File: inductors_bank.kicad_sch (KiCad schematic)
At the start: 38 parts, among them K301 HF3F-L-12-1ZL2T, K302 HF3F-L-12-1ZL2T, K303 HF3F-L-12-1ZL2T, K304 HF3F-L-12-1ZL2T, K305 HF3F-L-12-1ZL2T, K306 HF3F-L-12-1ZL2T, K307 HF3F-L-12-1ZL2T, Q301 PMOS, Q302 PMOS, Q303 NMOS, Q304 NMOS

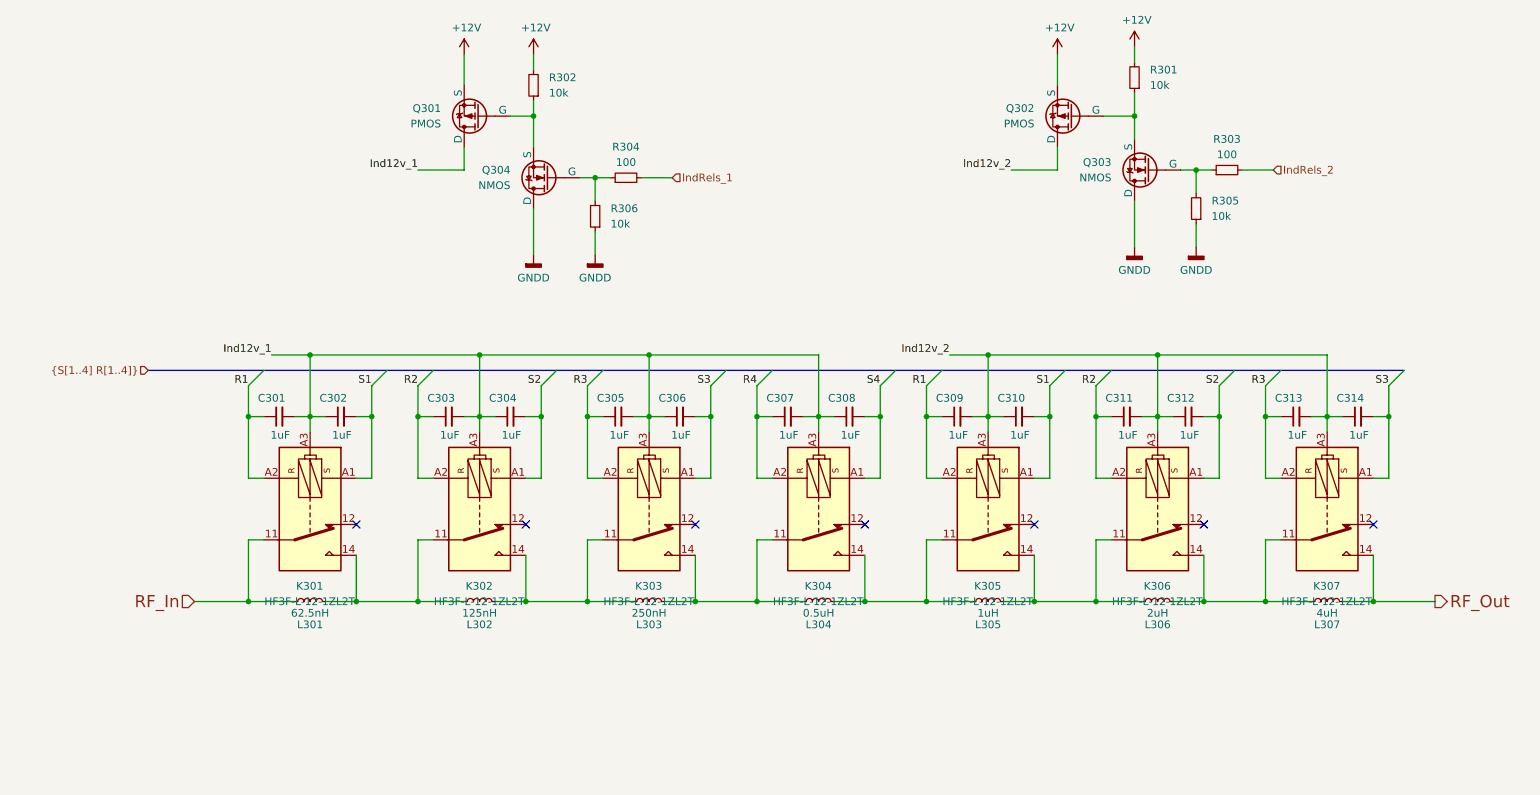
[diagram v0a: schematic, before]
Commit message: Added comments for inductors structure
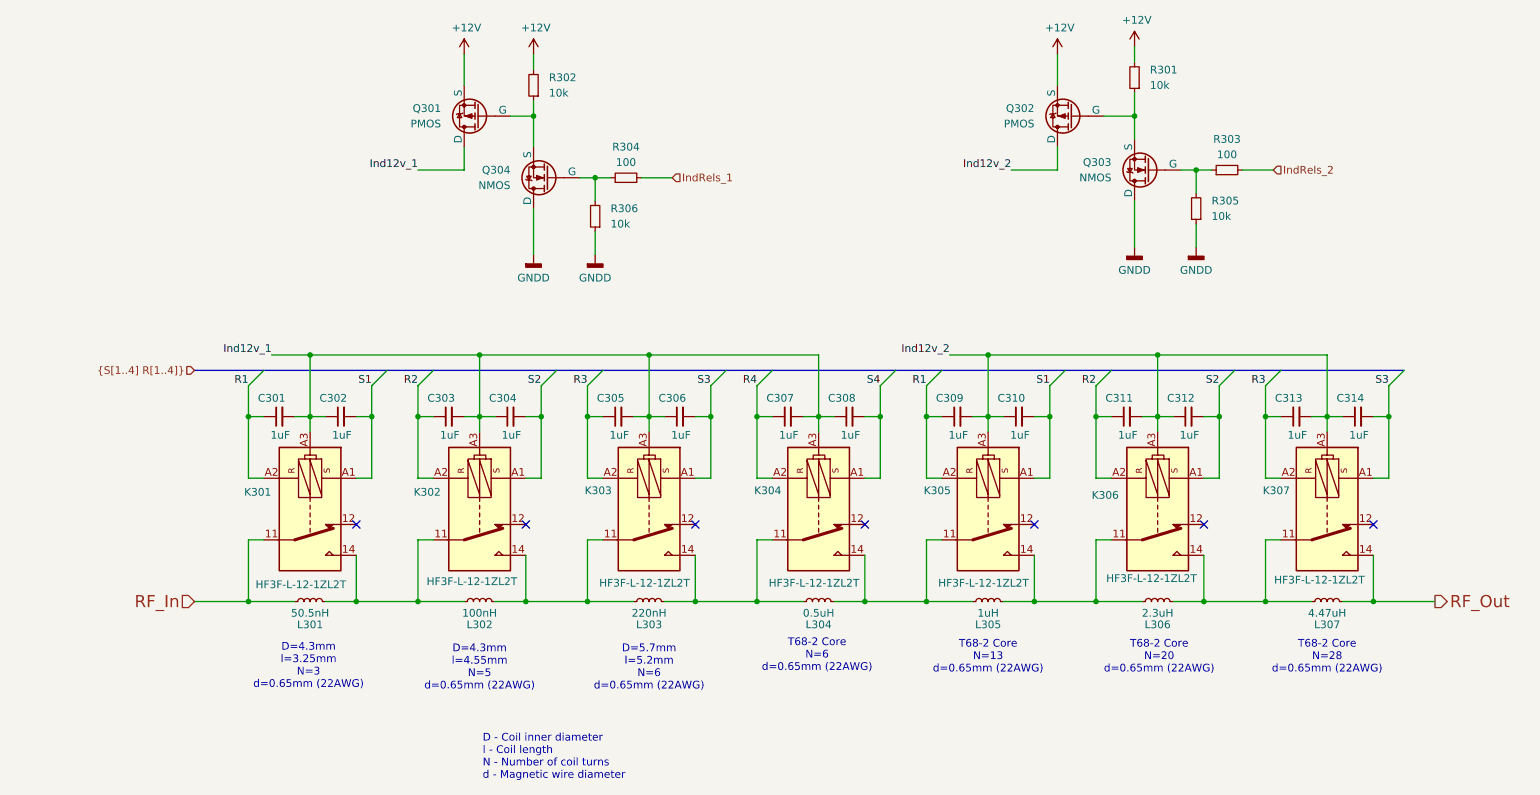
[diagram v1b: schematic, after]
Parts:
- L301: value 62.5nH -> 50.5nH
- L302: value 125nH -> 100nH
- L303: value 250nH -> 220nH
- L306: value 2uH -> 2.3uH
- L307: value 4uH -> 4.47uH
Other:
- note added: "D - Coil inner diameter l - Coil length N - Number of coil turns d - Magnetic wire diameter"
- note added: "D=4.3mm l=3.25mm N=3 d=0.65mm (22AWG)"
- note added: "D=4.3mm l=4.55mm N=5 d=0.65mm (22AWG)"
- note added: "D=5.7mm l=5.2mm N=6 d=0.65mm (22AWG)"
- note added: "T68-2 Core N=13 d=0.65mm (22AWG)"
- note added: "T68-2 Core N=20 d=0.65mm (22AWG)"
- note added: "T68-2 Core N=28 d=0.65mm (22AWG)"
- note added: "T68-2 Core N=6 d=0.65mm (22AWG)"
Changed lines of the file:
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@@
 	(bus
 		(pts
-			(xy 35.56 109.22) (xy 54.61 109.22)
+			(xy 43.18 109.22) (xy 54.61 109.22)
 		)
 		(stroke
@@
 		)
 	)
+	(text "D=5.7mm\nl=5.2mm\nN=6\nd=0.65mm (22AWG)"
+		(exclude_from_sim no)
+		(at 118.11 158.242 0)
+		(effects
+			(font
+				(size 1.27 1.27)
+			)
+		)
+	)
+	(text "D=4.3mm\nl=4.55mm\nN=5\nd=0.65mm (22AWG)"
+		(exclude_from_sim no)
+		(at 90.17 158.242 0)
+		(effects
+			(font
+				(size 1.27 1.27)
+			)
+		)
+	)
+	(text "D=4.3mm\nl=3.25mm\nN=3\nd=0.65mm (22AWG)"
+		(exclude_from_sim no)
+		(at 61.976 157.988 0)
+		(effects
+			(font
+				(size 1.27 1.27)
+			)
+		)
+	)
+	(text "T68-2 Core\nN=6\nd=0.65mm (22AWG)"
+		(exclude_from_sim no)
+		(at 145.796 156.21 0)
+		(effects
+			(font
+				(size 1.27 1.27)
+			)
+		)
+	)
+	(text "D - Coil inner diameter\nl - Coil length\nN - Number of coil turns\nd - Magnetic wire diameter"
+		(exclude_from_sim no)
+		(at 90.678 172.974 0)
+		(effects
+			(font
+				(size 1.27 1.27)
+			)
+			(justify left)
+		)
+	)
+	(text "T68-2 Core\nN=28\nd=0.65mm (22AWG)"
+		(exclude_from_sim no)
+		(at 229.87 156.464 0)
+		(effects
+			(font
+				(size 1.27 1.27)
+			)
+		)
+	)
+	(text "T68-2 Core\nN=20\nd=0.65mm (22AWG)"
+		(exclude_from_sim no)
+		(at 202.184 156.464 0)
+		(effects
+			(font
+				(size 1.27 1.27)
+			)
+		)
+	)
+	(text "T68-2 Core\nN=13\nd=0.65mm (22AWG)"
+		(exclude_from_sim no)
+		(at 173.99 156.464 0)
+		(effects
+			(font
+				(size 1.27 1.27)
+			)
+		)
+	)
 	(label "S2"
 		(at 212.09 111.76 180)
@@
 	(hierarchical_label "{S[1..4] R[1..4]}"
 		(shape input)
-		(at 35.56 109.22 180)
+		(at 43.18 109.22 180)
 		(fields_autoplaced yes)
 		(effects
@@
 		(on_board yes)
 		(dnp no)
-		(fields_autoplaced yes)
 		(property "Reference" "K301"
-			(at 62.1665 144.78 90)
+			(at 53.594 129.286 90)
 			(effects
 				(font
@@
 		)
 		(property "Value" "HF3F-L-12-1ZL2T"
-			(at 62.1665 147.32 90)
+			(at 60.706 144.526 90)
 			(effects
 				(font
@@
 			)
 		)
-		(property "Value" "4uH"
+		(property "Value" "4.47uH"
 			(at 229.87 149.225 90)
 			(effects
@@
 			)
 		)
-		(property "Value" "2uH"
+		(property "Value" "2.3uH"
 			(at 201.93 149.225 90)
 			(effects
@@
 			)
 		)
-		(property "Value" "250nH"
+		(property "Value" "220nH"
 			(at 118.11 149.225 90)
 			(effects
@@
 		(on_board yes)
 		(dnp no)
-		(fields_autoplaced yes)
 		(property "Reference" "K302"
-			(at 90.1065 144.78 90)
+			(at 81.534 129.286 90)
 			(effects
 				(font
@@
 		)
 		(property "Value" "HF3F-L-12-1ZL2T"
-			(at 90.1065 147.32 90)
+			(at 88.9 144.018 90)
 			(effects
 				(font
@@
 			)
 		)
-		(property "Value" "125nH"
+		(property "Value" "100nH"
 			(at 90.17 149.225 90)
 			(effects
@@
 		(on_board yes)
 		(dnp no)
-		(fields_autoplaced yes)
 		(property "Reference" "K304"
-			(at 145.9865 144.78 90)
+			(at 137.668 129.032 90)
 			(effects
 				(font
@@
 		)
 		(property "Value" "HF3F-L-12-1ZL2T"
-			(at 145.9865 147.32 90)
+			(at 145.288 144.272 90)
 			(effects
 				(font
@@
 		(on_board yes)
 		(dnp no)
-		(fields_autoplaced yes)
 		(property "Reference" "K307"
-			(at 229.8065 144.78 90)
+			(at 221.488 129.032 90)
 			(effects
 				(font
@@
 		)
 		(property "Value" "HF3F-L-12-1ZL2T"
-			(at 229.8065 147.32 90)
+			(at 228.6 143.764 90)
 			(effects
 				(font
@@
 		(on_board yes)
 		(dnp no)
-		(fields_autoplaced yes)
 		(property "Reference" "K305"
-			(at 173.9265 144.78 90)
+			(at 165.608 129.032 90)
 			(effects
 				(font
@@
 		)
 		(property "Value" "HF3F-L-12-1ZL2T"
-			(at 173.9265 147.32 90)
+			(at 173.228 144.272 90)
 			(effects
 				(font
@@
 			)
 		)
-		(property "Value" "62.5nH"
+		(property "Value" "50.5nH"
 			(at 62.23 149.225 90)
 			(effects
@@
 		(on_board yes)
 		(dnp no)
-		(fields_autoplaced yes)
 		(property "Reference" "K306"
-			(at 201.8665 144.78 90)
+			(at 193.294 129.794 90)
 			(effects
 				(font
@@
 		)
 		(property "Value" "HF3F-L-12-1ZL2T"
-			(at 201.8665 147.32 90)
+			(at 200.914 143.51 90)
 			(effects
 				(font
@@
 		(on_board yes)
 		(dnp no)
-		(fields_autoplaced yes)
 		(property "Reference" "K303"
-			(at 118.0465 144.78 90)
+			(at 109.728 129.032 90)
 			(effects
 				(font
@@
 		)
 		(property "Value" "HF3F-L-12-1ZL2T"
-			(at 118.0465 147.32 90)
+			(at 117.348 144.272 90)
 			(effects
 				(font

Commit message: Set footprints for inductors. Improved schematic of capcitors and inductors banks.
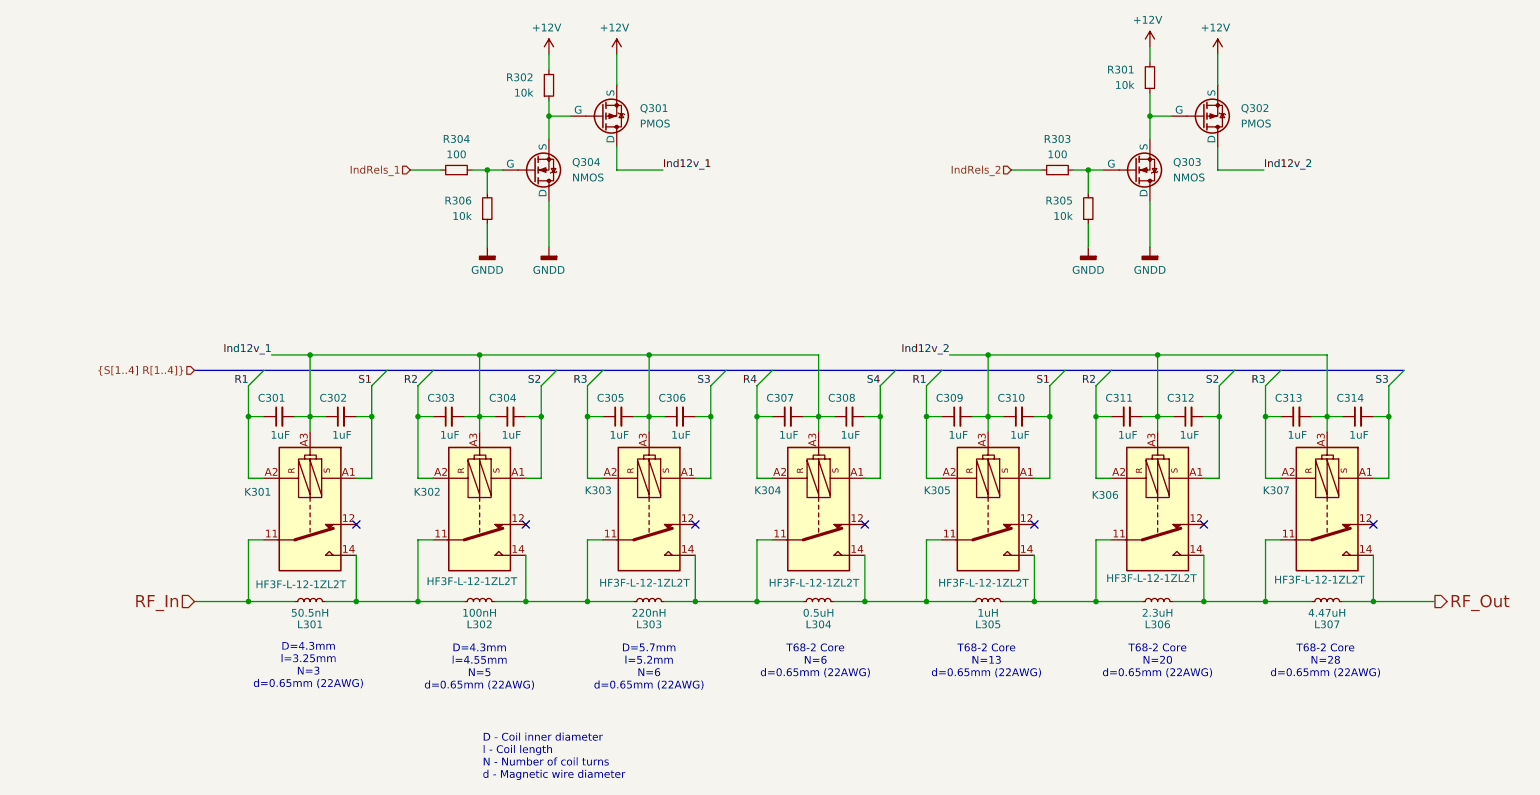
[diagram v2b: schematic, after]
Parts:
- L301: footprint My_KiCad_Libs:Toroid_Vertical_L19.5mm_W8.0mm_P7.5mm -> ZFTuner_Lib:Inductor_3DP_N3_L5.35mm_W6.3mm_P2.58mm
- L302: footprint My_KiCad_Libs:Toroid_Vertical_L19.5mm_W8.0mm_P7.5mm -> ZFTuner_Lib:Inductor_3DP_N5_L6.69mm_W6.3mm_P3.92mm
- L303: footprint My_KiCad_Libs:Toroid_Vertical_L19.5mm_W8.0mm_P7.5mm -> ZFTuner_Lib:Inductor_3DP_N6_L7.36mm_W7.7mm_P4.59mm
- L304, L305, L306, L307: footprint My_KiCad_Libs:Toroid_Vertical_L19.5mm_W8.0mm_P7.5mm -> ZFTuner_Lib:Toroid_Vertical_L19.5mm_W8.0mm_P7.5mm
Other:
- moved on the sheet: Q301, Q302, Q303, Q304, R301, R302, R303, R304, R305, R306

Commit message: Created PDF of schematic
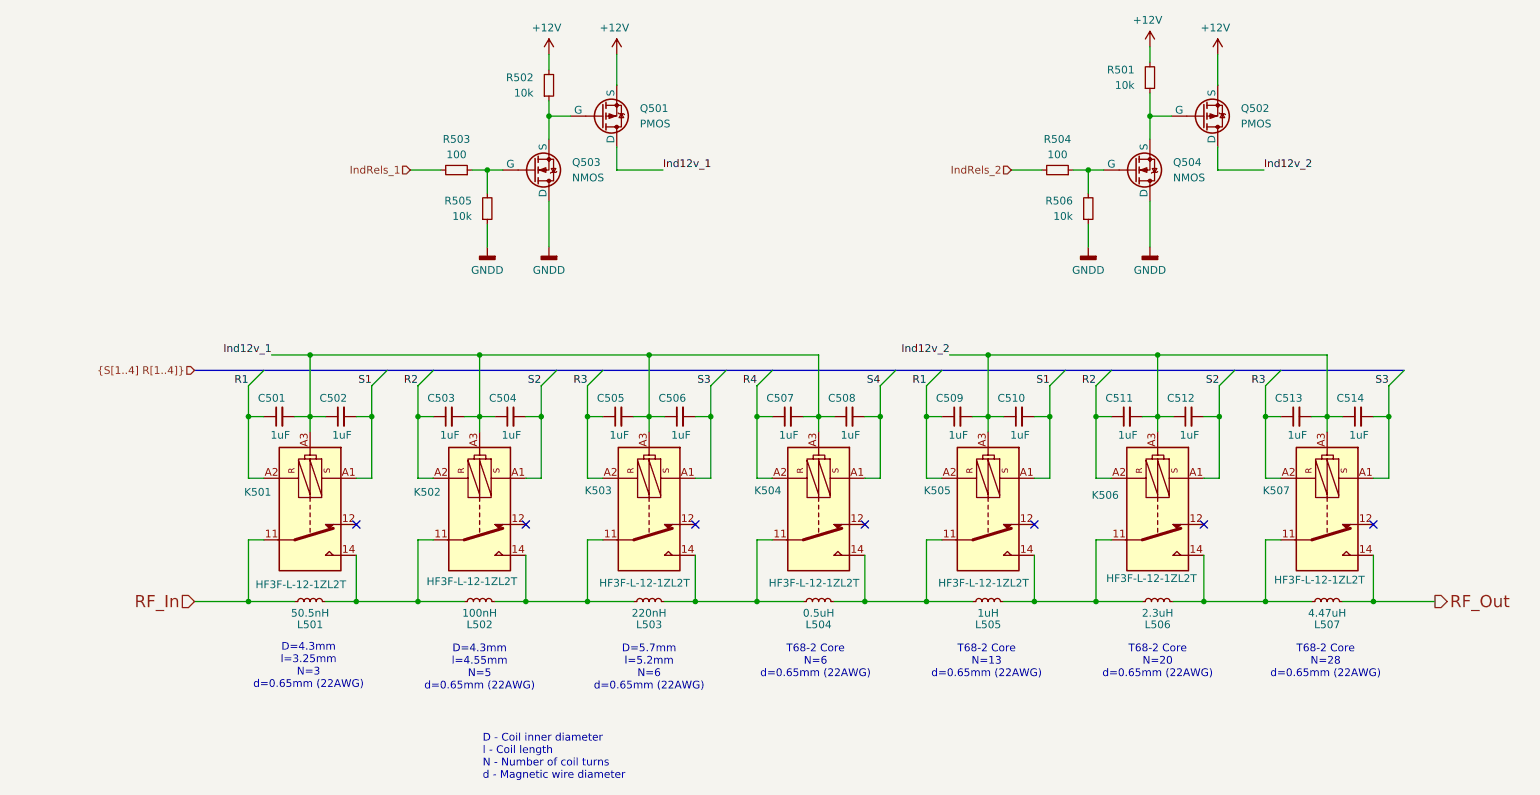
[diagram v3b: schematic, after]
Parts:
- renumbered C301 to C501, C302 to C502, C303 to C503, C304 to C504, C305 to C505, C306 to C506, C307 to C507, C308 to C508, C309 to C509, C310 to C510, C311 to C511, C312 to C512, C313 to C513, C314 to C514, K301 to K501, K302 to K502, K303 to K503, K304 to K504, K305 to K505, K306 to K506, K307 to K507, L301 to L501, L302 to L502, L303 to L503, L304 to L504, L305 to L505, L306 to L506, L307 to L507, Q301 to Q501, Q302 to Q502, Q304 to Q503, Q303 to Q504, R301 to R501, R302 to R502, R304 to R503, R303 to R504, R306 to R505, R305 to R506

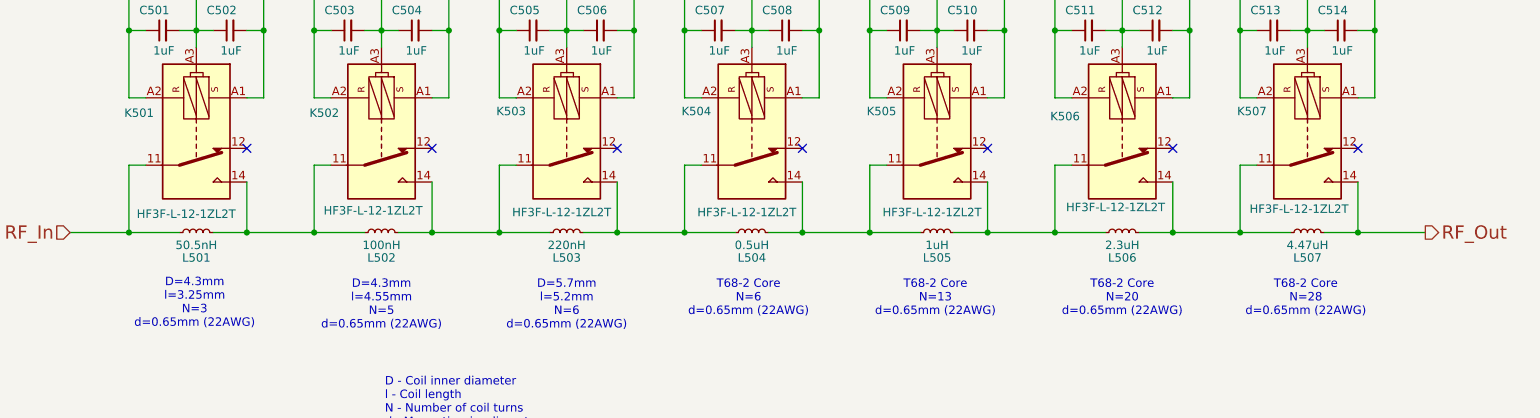
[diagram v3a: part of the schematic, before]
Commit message: Schematic fixes for PCB layout
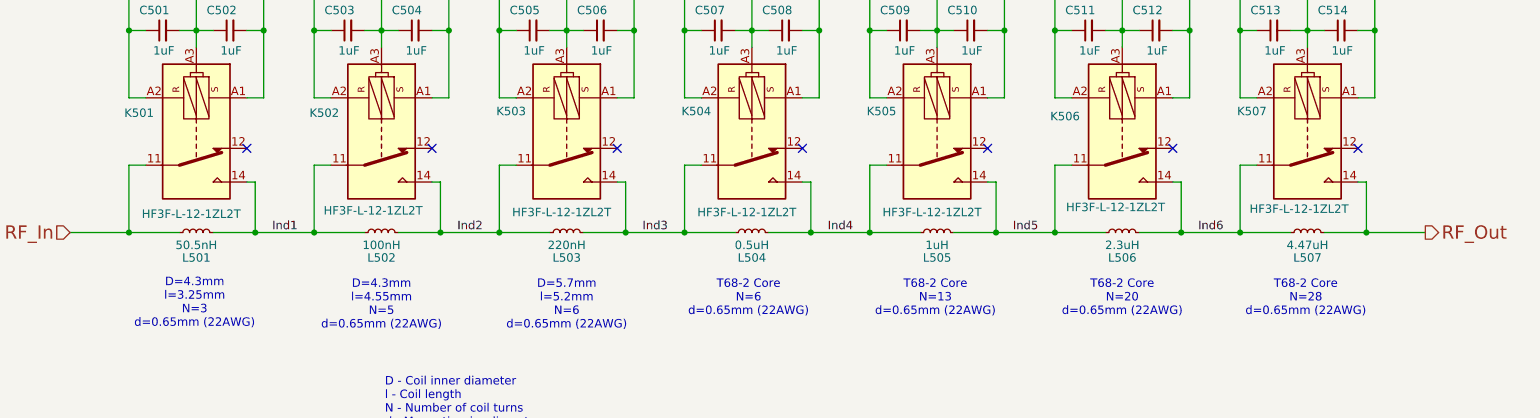
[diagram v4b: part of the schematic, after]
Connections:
- net Ind1: now reaches K501.14, K502.11, L501.2, L502.1
- net Ind6: now reaches K506.14, K507.11, L506.2, L507.1
- net Ind5: now reaches K505.14, K506.11, L505.2, L506.1
- net Ind2: now reaches K502.14, K503.11, L502.2, L503.1
- net Ind3: now reaches K503.14, K504.11, L503.2, L504.1
- net Ind4: now reaches K504.14, K505.11, L504.2, L505.1
